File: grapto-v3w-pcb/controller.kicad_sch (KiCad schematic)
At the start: 47 parts

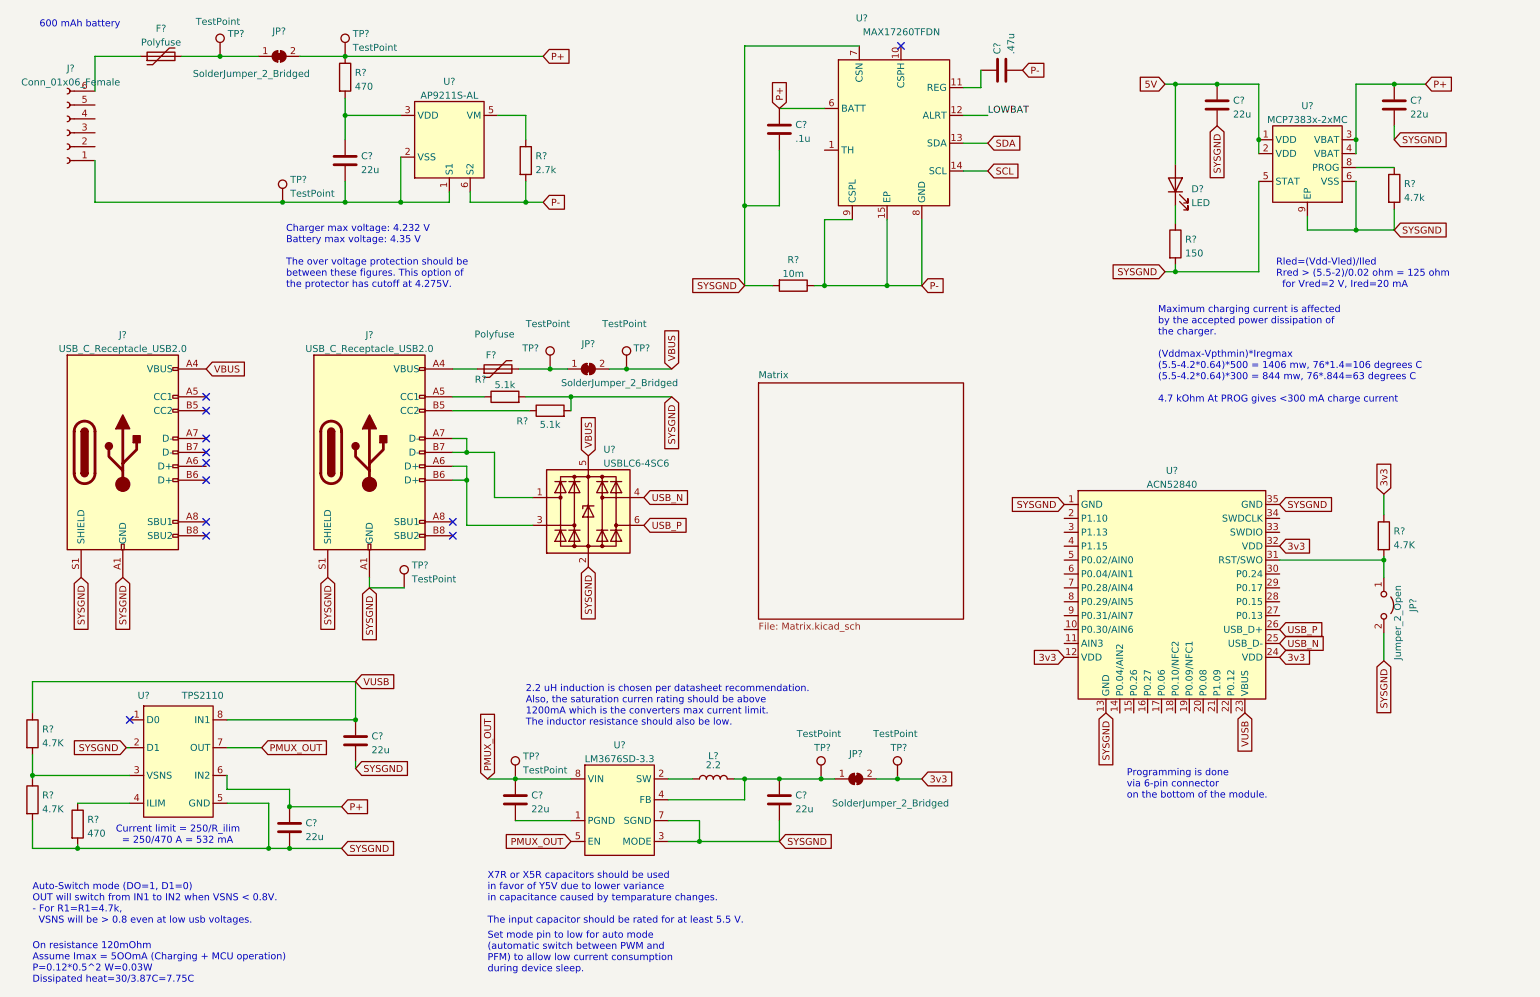
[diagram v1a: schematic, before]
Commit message: Added keymatrix.
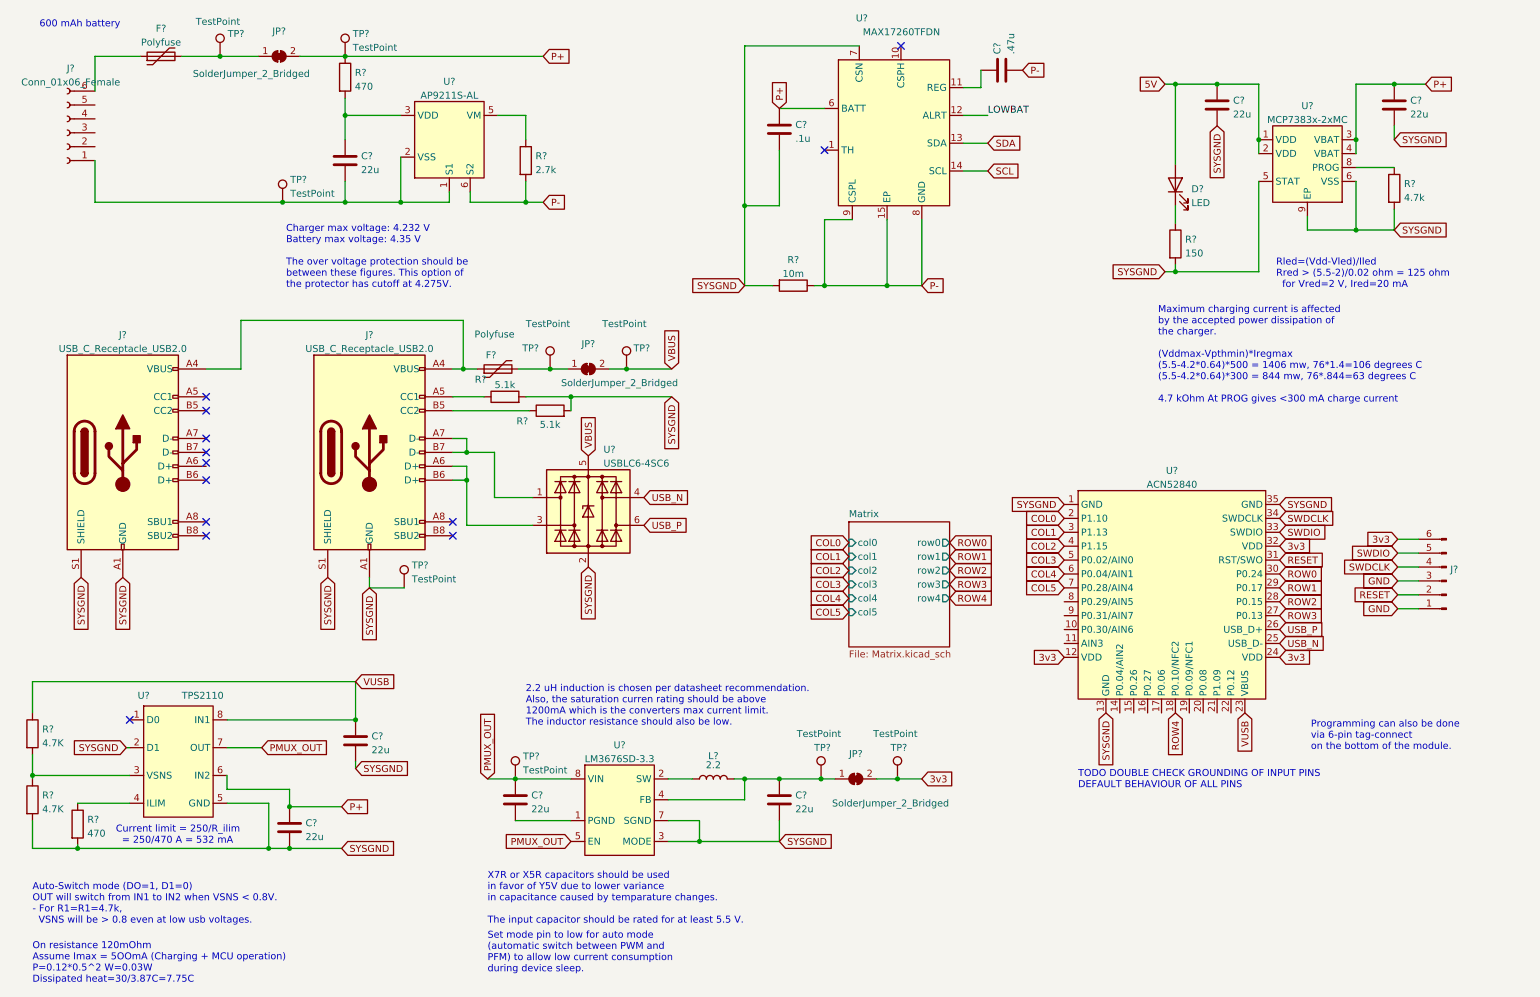
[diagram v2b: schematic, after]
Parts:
- removed JP?: Jumper_2_Open, symbol Jumper:Jumper_2_Open
- removed R?: 4.7K, symbol Device:R
- added J?: (no value), symbol Connector:Conn_01x06_Male
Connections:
- net 3v3: now also J?.6 (Pin_6)
- net VBUS: no longer J?.A4 (VBUS), J?.A9 (VBUS), J?.B4 (VBUS), J?.B9 (VBUS)
- net at F?.1, J?.A4 (VBUS), J?.A9 (VBUS)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: now also J?.A4 (VBUS), J?.A9 (VBUS), J?.B4 (VBUS), J?.B9 (VBUS)
- net ROW4: now reaches U?.18 (P0.10/NFC2)
- net COL0: now reaches U?.2 (P1.10)
- net ROW3: now reaches U?.27 (P0.13)
- net ROW2: now reaches U?.28 (P0.15)
- net ROW1: now reaches U?.29 (P0.17)
- net COL1: now reaches U?.3 (P1.13)
- net ROW0: now reaches U?.30 (P0.24)
- net RESET: now reaches U?.31 (RST/SWO)
- net RESET: now also J?.2 (Pin_2)
- net SWDIO: now reaches U?.33 (SWDIO)
- net SWDIO: now also J?.5 (Pin_5)
- net SWDCLK: now reaches U?.34 (SWDCLK)
- net SWDCLK: now also J?.4 (Pin_4)
- net COL2: now reaches U?.4 (P1.15)
- net COL3: now reaches U?.5 (P0.02/AIN0)
- net COL4: now reaches U?.6 (P0.04/AIN1)
- net COL5: now reaches U?.7 (P0.28/AIN4)
- new net GND: J?.1 (Pin_1), J?.3 (Pin_3)
- no-connect marks 12 -> 13
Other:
- sheet Matrix ports: added col0, col1, col2, col3, col4, col5, row0, row1, row2, row3, row4; removed none
- note added: "Programming can also be done via 6-pin tag-connect on the bottom of the module."
- note added: "TODO DOUBLE CHECK GROUNDING OF INPUT PINS DEFAULT BEHAVIOUR OF ALL PINS"
- note removed: "Programming is done via 6-pin connector on the bottom of the module."

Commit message: schematic soon finished.
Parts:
- added R10, R11, R7, R8: (no value), symbol Device:R
- gave numbers to parts that had none: 46
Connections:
- net 5V is gone; now on net VBUS: C2.1, D30.2 (A), U2.1 (VDD), U2.2 (VDD)
- net LOWBAT is gone; now on net LOWBATT: U1.12 (ALRT)
- net 3v3: now also R7.1, R8.1
- net GND: no longer J4.3 (Pin_3)
- net P-: no longer U1.15 (EP)
- net SCL: now also U5.16 (P0.27), R8.2
- net SDA: now also U5.15 (P0.26), R7.2
- net SYSGND: no longer J2.S1 (SHIELD), J3.S1 (SHIELD), U2.9 (EP)
- net USB_N: now also R10.2; no longer U4.4 (I/O3)
- net USB_P: now also R11.2; no longer U4.6 (I/O4)
- net STATUS: now reaches U5.21 (P1.09)
- net STATUS: now also J4.3 (Pin_3)
- net LOWBATT: now reaches U5.8 (P0.29/AIN5)
- net C-: now reaches C5.2, J1.1 (Pin_1), TP3.1, U3.1 (S1), U3.2 (VSS)
- net C+: now reaches F1.1, J1.6 (Pin_6)
- new net: R10.1, U4.4 (I/O3)
- new net: R11.1, U4.6 (I/O4)
- new net CHASSI: J2.S1 (SHIELD), J3.S1 (SHIELD), U1.15 (EP), U2.9 (EP)
- no-connect marks 13 -> 25
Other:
- note added: "Before using battery protector, VM must be connected to P- or C- to activate it. Otherwise battery cannot discharge."
- note added: "Charger max voltage: 4.232 V, Battery max voltage: 4.35 V The over voltage protection should be between these figures. This option of the protector has cutoff at 4.275V."
- note added: "Fuse: I_hold = 0.75 A, I_trip = 1.5 A"
- note added: "I2C @ 100 kbps Don't know the parasitic trace capacitance so Pull-ups have to tested."
- note added: "SDA and SCL can be mapped to any GPIO"
- note removed: "Charger max voltage: 4.232 V Battery max voltage: 4.35 V The over voltage protection should be between these figures. This option of the protector has cutoff at 4.275V."
- moved on the sheet: C5, F1, J1, JP1, R1, R2, TP1, TP2, TP3, U3

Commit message: Footprints done.
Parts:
- removed C1: .47u, symbol Device:C
- removed C2, C3, C5: 22u, symbol Device:C
- removed C4: .1u, symbol Device:C
- removed D30: LED, symbol Device:LED
- removed F1: Polyfuse, symbol Device:Polyfuse
- removed JP1: SolderJumper_2_Bridged, symbol Jumper:SolderJumper_2_Bridged
- removed R1: 470, symbol Device:R
- removed R2: 2.7k, symbol Device:R
- removed R3: 4.7k, symbol Device:R
- removed R4: 150, symbol Device:R
- removed R5: 10m, symbol Device:R
- removed TP1, TP2, TP3: TestPoint, symbol Connector:TestPoint
- removed U1: MAX17260TFDN, symbol grapto-v3w:MAX17260TFDN
- removed U2: MCP7383x-2xMC, symbol grapto-v3w:MCP7383x-2xMC
- removed U3: AP9211S-AL, symbol grapto-v3w:AP9211S-AL
- J8: renamed from J4; value (none) -> Conn_01x06_Male
- R21: renamed from R7; value (none) -> 10k
- R22: renamed from R8; value (none) -> 10k
- R24: renamed from R10; value (none) -> 22
- R25: renamed from R11; value (none) -> 22
- U13: renamed from U6; value TPS2110 -> (none)
- U14: renamed from U7; value LM3676SD-3.3 -> (none)
- renumbered C6 to C15, C7 to C16, C8 to C17, C9 to C18, F2 to F4, J2 to J6, J3 to J7, JP2 to JP5, JP3 to JP6, L1 to L2, R6 to R20, R9 to R23, R12 to R26, R13 to R27, R14 to R28, TP4 to TP13, TP5 to TP14, TP6 to TP15, TP7 to TP16, TP8 to TP17, TP9 to TP18, U4 to U11, U5 to U12
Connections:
- net GND is gone; now on net sysgnd: J8.1 (Pin_1)
- net SYSGND is gone; now on net sysgnd: C15.2, C17.2, C18.2, J6.A1 (GND), J6.A12 (GND), J6.B1 (GND), J6.B12 (GND), J7.A1 (GND), J7.A12 (GND), J7.B1 (GND), J7.B12 (GND), R20.2, R23.2, R27.2, R28.2, TP15.1, U11.2 (GND), U12.1 (GND), U12.13 (GND), U12.35 (GND), U13.2 (D1), U13.5 (GND), U14.3 (MODE), U14.7 (SGND)
- net VUSB is gone; now on net vusb: C15.1, R26.1, U12.23 (VBUS), U13.8 (IN1)
- net sysgnd: now reaches C16.2, U14.1 (PGND)
- net 3v3 renamed 3.3v
- net C+ renamed BatteryManagement/batt+
- net C- renamed BatteryManagement/batt-
- net CHASSI renamed chassi
- net COL0 renamed col0
- net COL1 renamed col1
- net COL2 renamed col2
- net COL3 renamed col3
- net COL4 renamed col4
- net COL5 renamed col5
- net LOWBATT renamed low_batt
- net P+ renamed p+
- net PMUX_OUT renamed pmux_out
- net RESET renamed reset
- net ROW0 renamed row0
- net ROW1 renamed row1
- net ROW2 renamed row2
- net ROW3 renamed row3
- net ROW4 renamed row4
- net SCL renamed scl
- net scl: now also R21.2; no longer R22.2
- net SDA renamed sda
- net sda: now also R22.2; no longer R21.2
- net STATUS renamed status
- net SWDCLK renamed swdclk
- net SWDIO renamed swdio
- net USB_N renamed usb_n
- net USB_P renamed usb_p
- net VBUS renamed vusb
- no-connect marks 25 -> 23
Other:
- added sheet BatteryManagement (battery_management.kicad_sch)
- note added: "On resistance 120mOhm Assume Imax = 5OOmA P=0.12*0.5^2 W=0.03W Dissipated heat=30/3.87C=7.75C"
- note removed: "600 mAh battery"
- note removed: "Before using battery protector, VM must be connected to P- or C- to activate it. Otherwise battery cannot discharge."
- note removed: "Charger max voltage: 4.232 V, Battery max voltage: 4.35 V The over voltage protection should be between these figures. This option of the protector has cutoff at 4.275V."
- note removed: "Fuse: I_hold = 0.75 A, I_trip = 1.5 A"
- note removed: "Maximum charging current is affected by the accepted power dissipation of the charger. (Vddmax-Vpthmin)*Iregmax (5.5-4.2*0.64)*500 = 1406 mw, 76*1.4=106 degrees C (5.5-4.2*0.64)*300 = 844 mw, 76*.844=63 degrees C 4.7 kOhm At PROG gives <300 mA charge current"
- note removed: "On resistance 120mOhm Assume Imax = 5OOmA (Charging + MCU operation) P=0.12*0.5^2 W=0.03W Dissipated heat=30/3.87C=7.75C"
- note removed: "Rled=(Vdd-Vled)/Iled Rred > (5.5-2)/0.02 ohm = 125 ohm for Vred=2 V, Ired=20 mA"
- moved on the sheet: C15, C16, C17, C18, F4, J6, J7, J8, JP5, JP6, L2, R20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

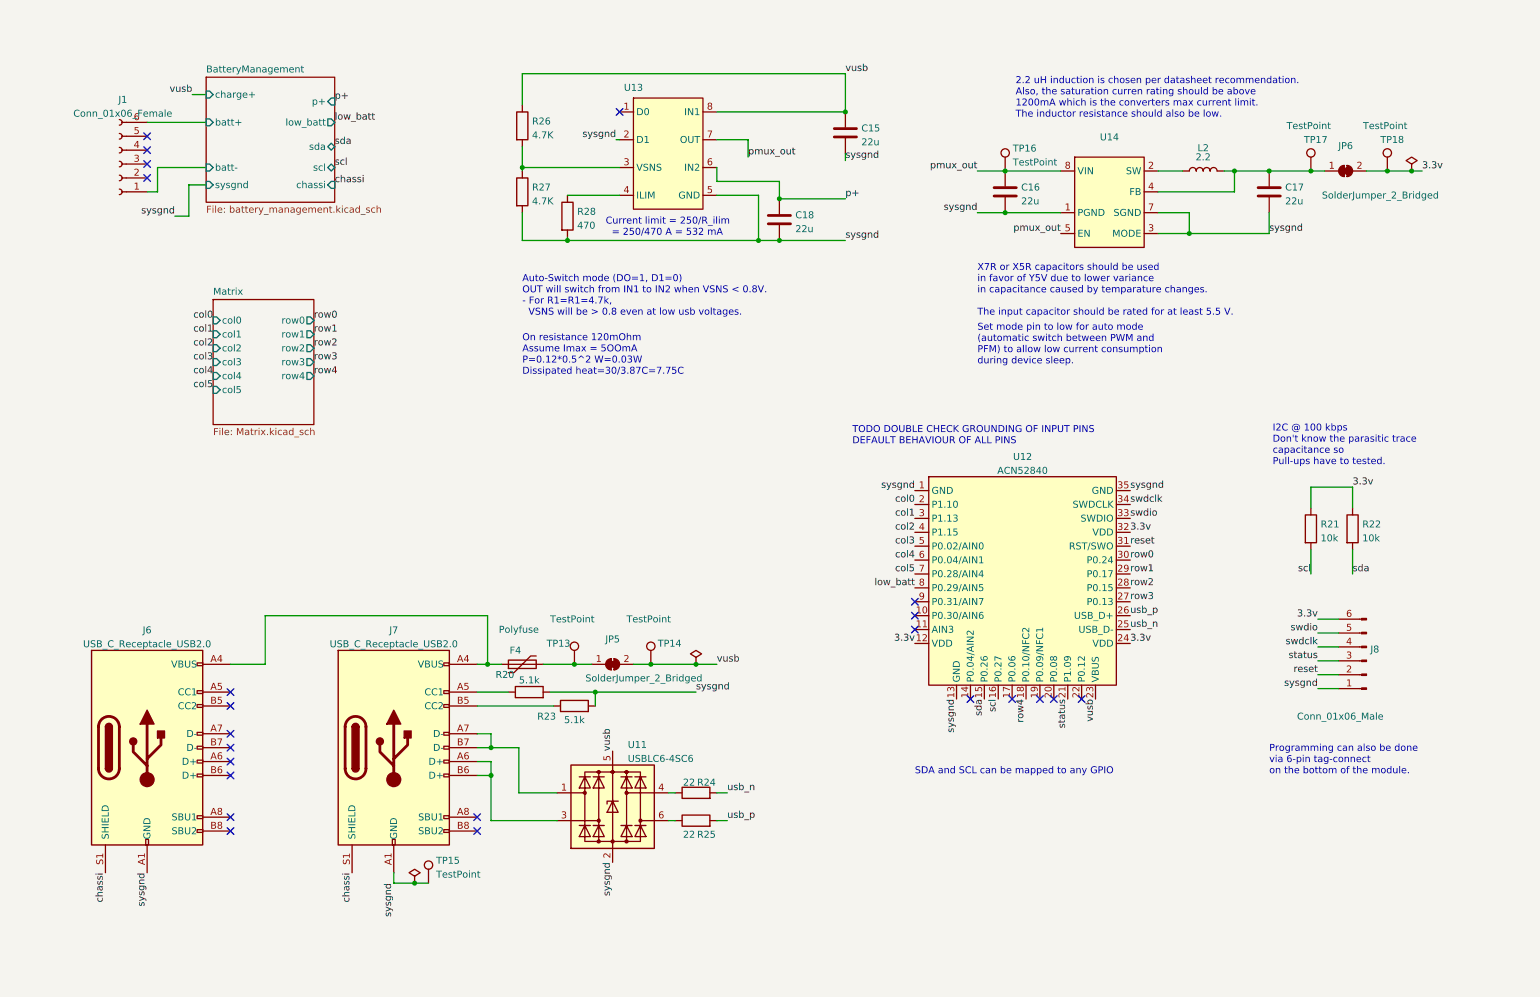
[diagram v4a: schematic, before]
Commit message: Fixed 3d model paths for pcb.
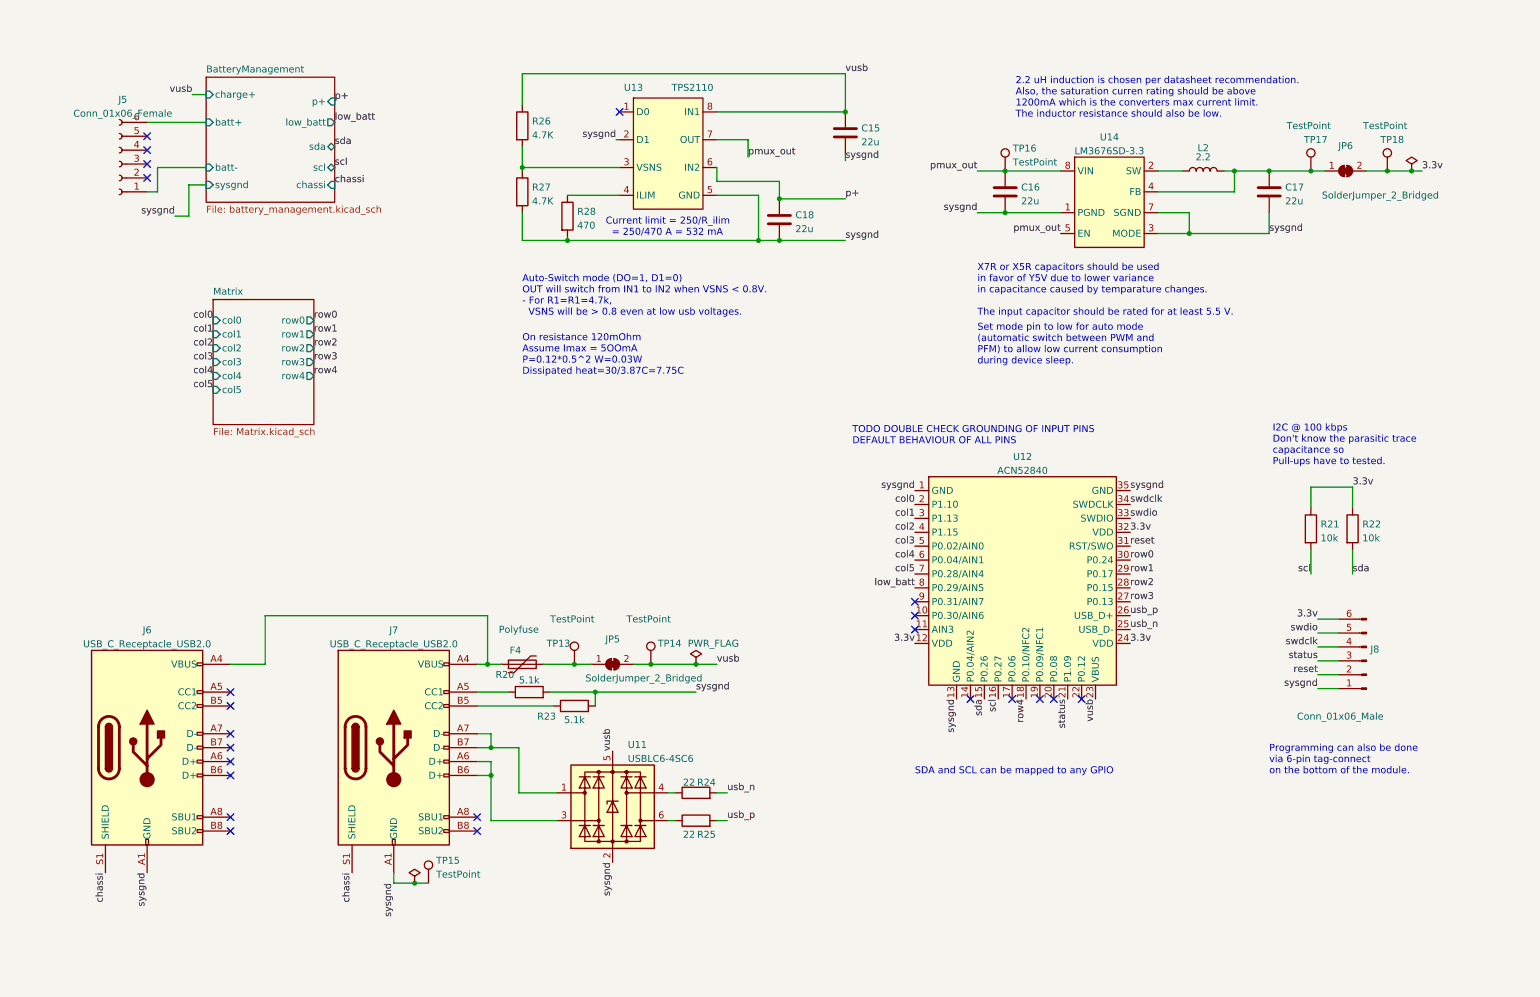
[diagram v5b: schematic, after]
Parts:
- C15, C16, C17, C18, F4: footprint (none) -> Fuse:Fuse_0603_1608Metric_Pad1.05x0.95mm_HandSolder
- J5: renamed from J1; footprint (none) -> grapto-v3w:df65-6P-1.7V
- J6: footprint (none) -> grapto-v3w:USB_C_Receptacle_molex_2169900001
- J8: footprint (none) -> Connector_PinHeader_2.54mm:PinHeader_1x06_P2.54mm_Vertical
- JP5, JP6: footprint (none) -> Jumper:SolderJumper-2_P1.3mm_Bridged_RoundedPad1.0x1.5mm
- L2: footprint (none) -> grapto-v3w:Bourns-SRP0415
- R20, R21, R22, R23, R24, R25, R26, R27, R28: footprint (none) -> Resistor_SMD:R_0603_1608Metric_Pad0.98x0.95mm_HandSolder
- TP13, TP14, TP15, TP16, TP17, TP18: footprint (none) -> TestPoint:TestPoint_Pad_2.0x2.0mm
- U12: footprint (none) -> grapto-v3w:ACN52840_mirror
- U13: value (none) -> TPS2110; footprint (none) -> Package_SO:TSSOP-8_4.4x3mm_P0.65mm
- U14: value (none) -> LM3676SD-3.3; footprint (none) -> Package_SON:WSON-8-1EP_3x3mm_P0.5mm_EP1.6x2.0mm
